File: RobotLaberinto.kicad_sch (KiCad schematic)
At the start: 33 parts, among them J1 VL53LDK, J2 VL53LDK, J3 VL53LDK, J4 VL53LDK, J5 VL53LDK, J6 BNO08, U1 DRV8833PWP, U2 ESP32-C3_SUPERMINI_TH, U3 MP2307, U4 CNY70

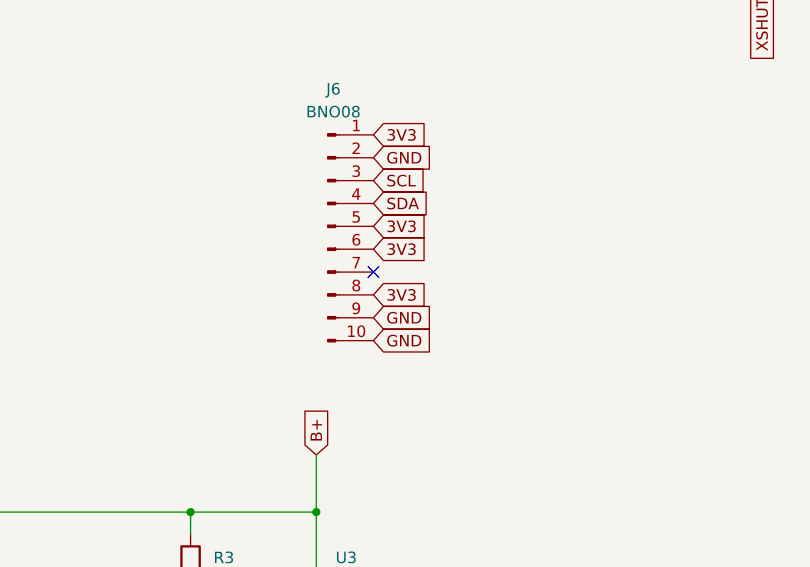
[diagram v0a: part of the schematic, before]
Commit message: correccion BNO
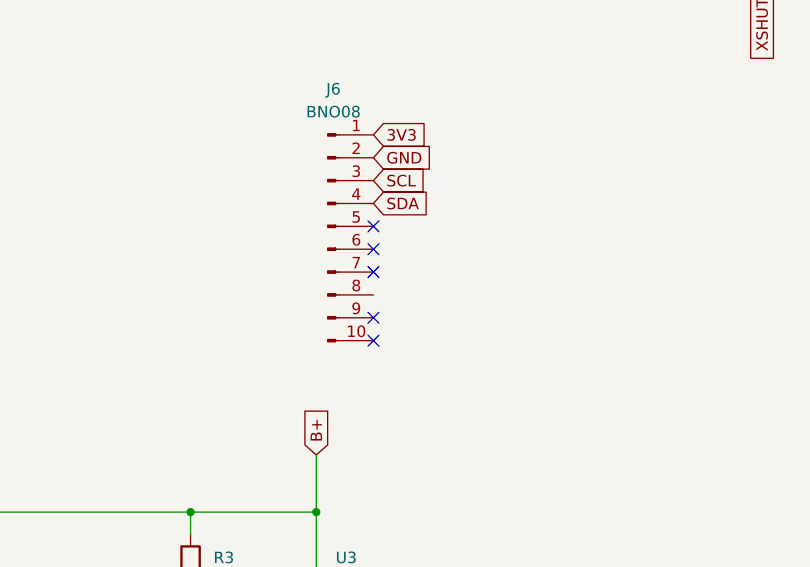
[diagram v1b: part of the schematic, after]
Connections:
- net 3V3: no longer J6.5 (Pin_5), J6.6 (Pin_6), J6.8 (Pin_8)
- net GND: no longer J6.10 (Pin_10), J6.9 (Pin_9)
- no-connect marks 4 -> 8

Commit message: trazado
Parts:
- added C10: 10n, Capacitor_SMD:C_0805_2012Metric_Pad1.18x1.45mm_HandSolder, symbol Device:C
- C1: footprint (none) -> Capacitor_SMD:C_0805_2012Metric_Pad1.18x1.45mm_HandSolder
- C3, C6: footprint Capacitor_SMD:C_0805_2012Metric_Pad1.18x1.45mm_HandSolder -> (none)
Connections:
- net SCL: now also U2.6 (GPIO6)
- net SDA: now also U2.5 (GPIO5)
- net at L1.1, U3.3 (SW): now also C10.1
- net at U3.1 (BS): now also C10.2
- no-connect marks 8 -> 9
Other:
- moved on the sheet: C6, L1, RV1, U2
